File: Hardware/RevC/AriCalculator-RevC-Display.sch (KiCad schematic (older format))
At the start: 15 parts, among them IC3 MCP1643

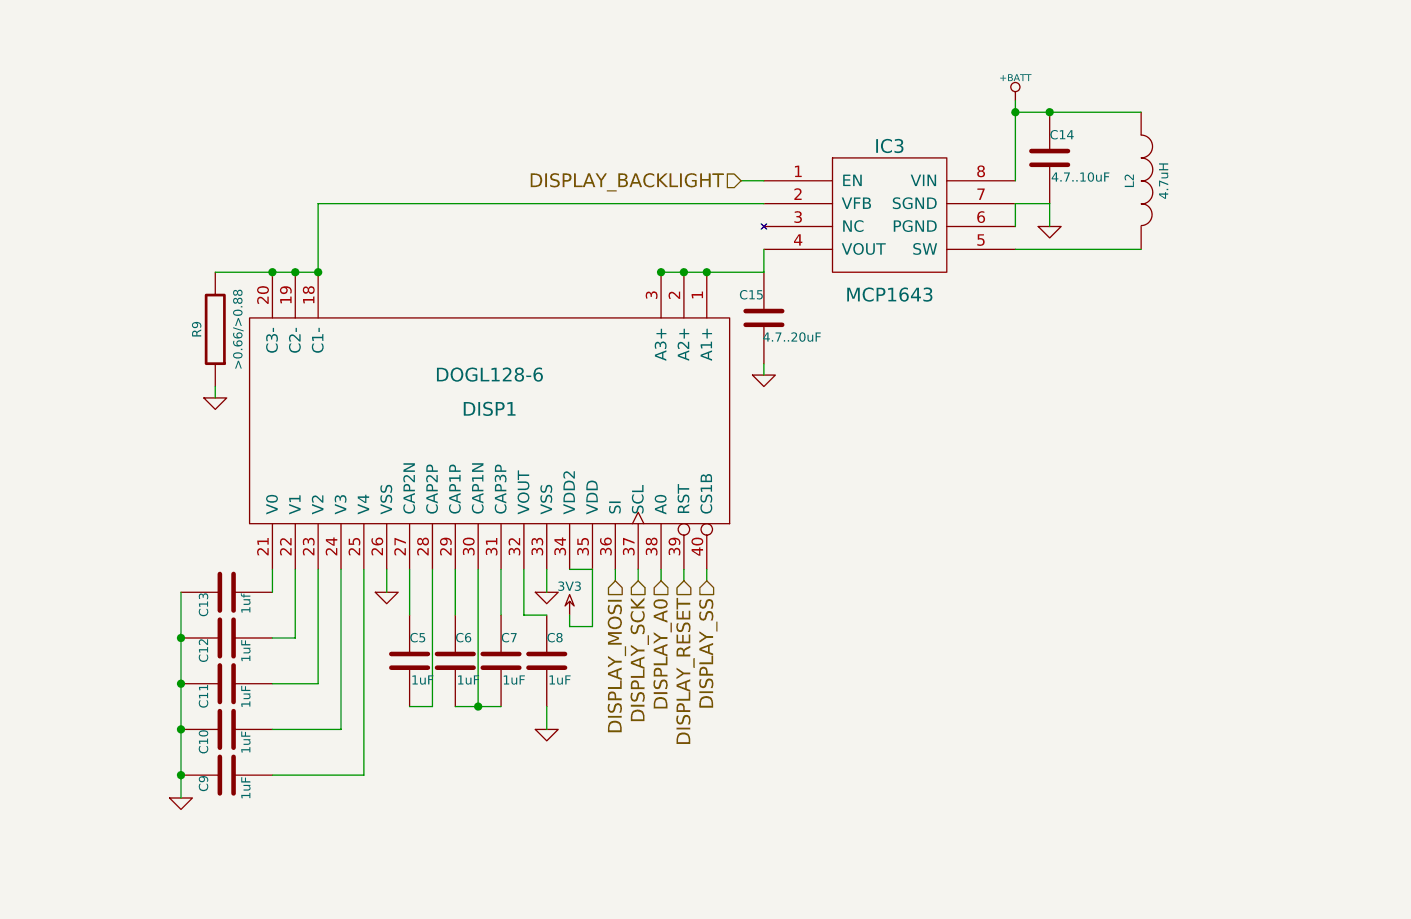
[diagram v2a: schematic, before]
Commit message: started RevC layout
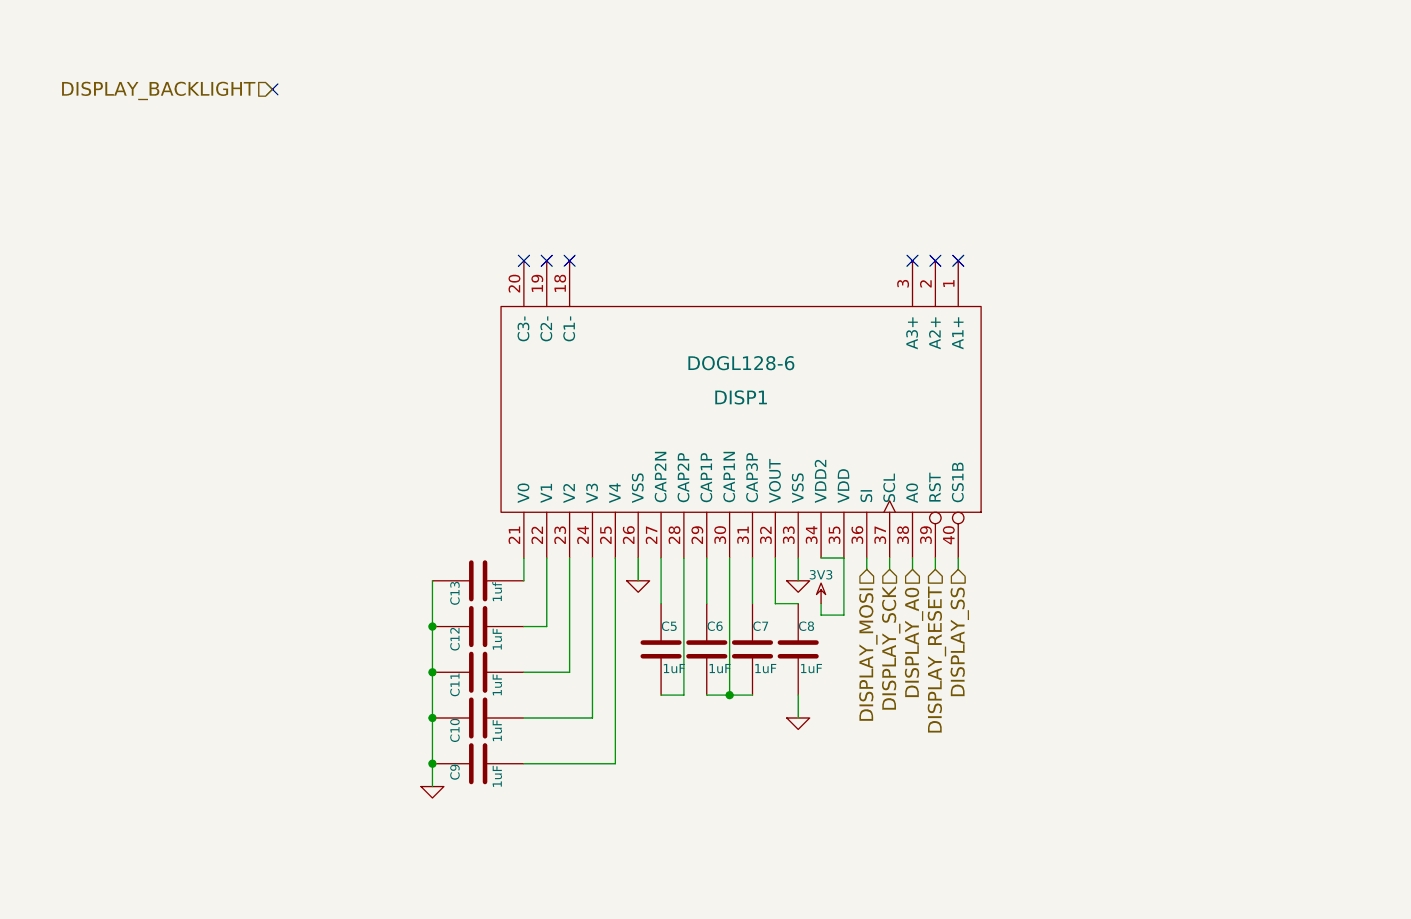
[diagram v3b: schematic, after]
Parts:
- removed C14: 4.7..10uF, ~, symbol C
- removed C15: 4.7..20uF, ~, symbol C
- removed IC3: MCP1643, symbol MCP1643
- removed L2: 4.7uH, ~, symbol INDUCTOR
- removed R9: >0.66/>0.88, ~, symbol R
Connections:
- now unconnected: DISP1.1 (A1+), DISP1.18 (C1-), DISP1.19 (C2-), DISP1.2 (A2+), DISP1.20 (C3-), DISP1.3 (A3+)
- no-connect marks 0 -> 7
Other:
- moved on the sheet: C10, C11, C12, C13, C5, C6, C7, C8, C9, DISP1

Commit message: work in progress
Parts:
- added C19: 10uF, ~, symbol C
- added C20: 20uF, ~, symbol C
- added IC4: MCP1643, ~, symbol MCP1643
- added L2: 4.7uH, ~, symbol INDUCTOR
- added LED10, LED11, LED12, LED13, LED14, LED15, LED16, LED17, LED18, LED19, LED4, LED5, LED6, LED7, LED8, LED9: BACKLIGHT, ~, symbol LED
- added LED20, LED21: IR, ~, symbol LED
- added R14: 0.66, ~, symbol R
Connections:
- net labels added: +BATT
- wire segments 31 -> 54
- no-connect marks 7 -> 0
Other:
- moved on the sheet: C10, C11, C12, C13, C5, C6, C7, C8, C9, DISP1

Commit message: work in progress
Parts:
- LED20, LED21: value IR -> BACKLIGHT
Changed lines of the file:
@@
 Sheet 4 6
 Title "Display"
-Date "12 nov 2014"
+Date "15 nov 2014"
 Rev "RevC"
 Comp "Dirk Heisswolf"
@@
 P 6650 1800
 F 0 "LED20" H 6650 1900 50  0000 C CNN
-F 1 "IR" H 6650 1700 50  0000 C CNN
+F 1 "BACKLIGHT" H 6650 1700 50  0000 C CNN
 F 2 "~" H 6650 1800 60  0000 C CNN
 F 3 "~" H 6650 1800 60  0000 C CNN
@@
 P 6950 1800
 F 0 "LED21" H 6950 1900 50  0000 C CNN
-F 1 "IR" H 6950 1700 50  0000 C CNN
+F 1 "BACKLIGHT" H 6950 1700 50  0000 C CNN
 F 2 "~" H 6950 1800 60  0000 C CNN
 F 3 "~" H 6950 1800 60  0000 C CNN
